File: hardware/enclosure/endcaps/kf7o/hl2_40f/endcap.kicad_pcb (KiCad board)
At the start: 2 copper layers, 106 x 40 mm, 22 parts, among them U1 IS31AP4996

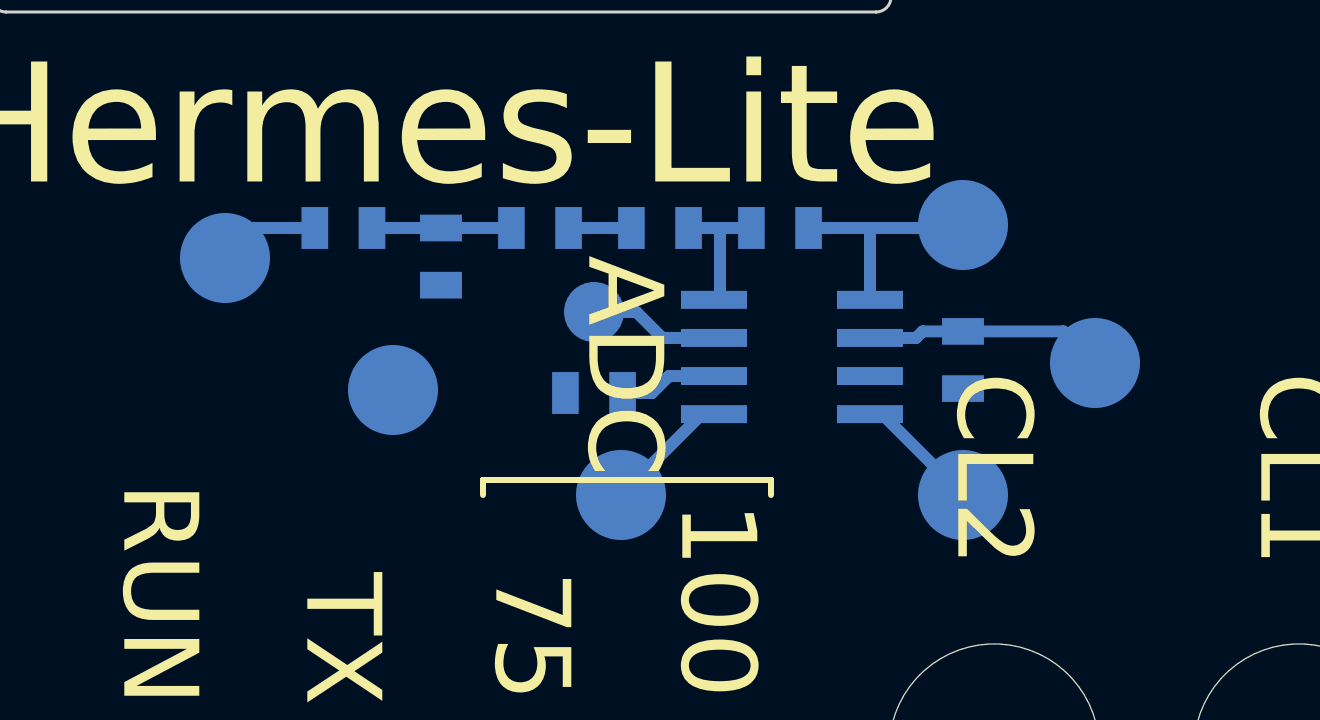
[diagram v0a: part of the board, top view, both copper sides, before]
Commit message: Add LPF for fan on latest end plates
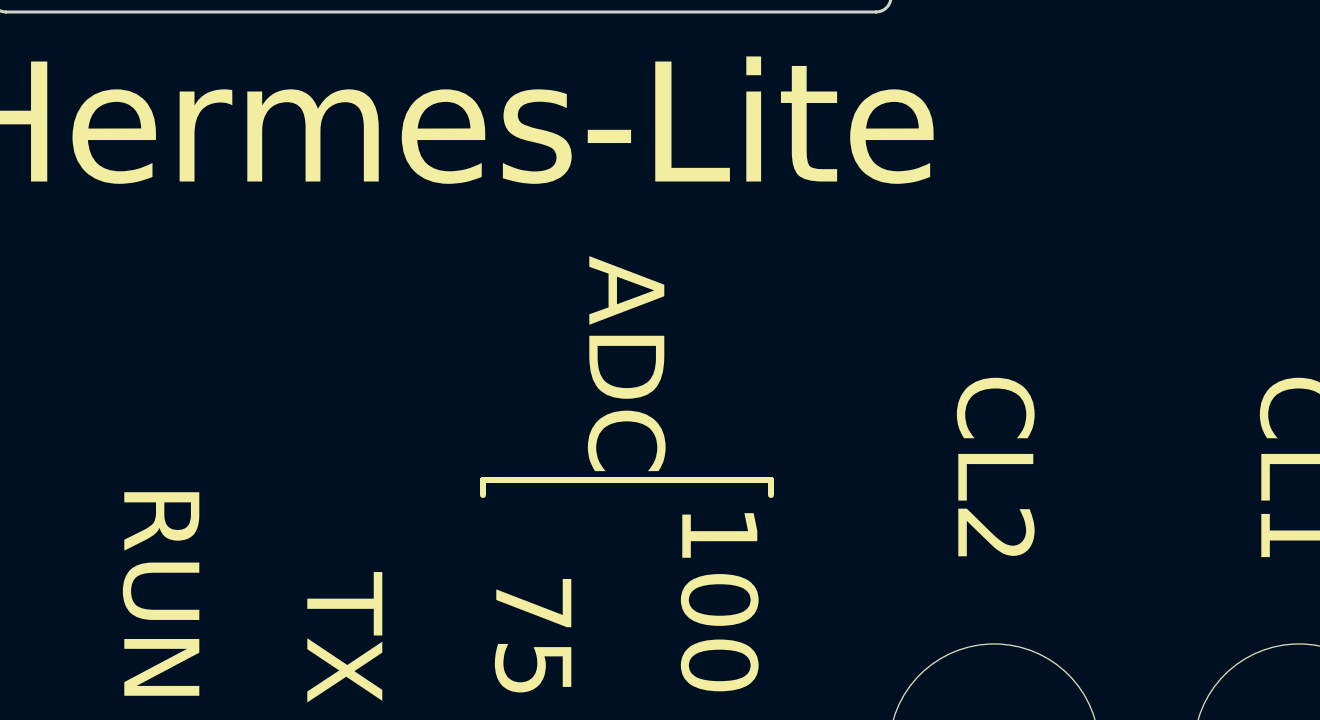
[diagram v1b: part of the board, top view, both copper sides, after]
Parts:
- removed C1, C4: 1uF, endcaplib:SMD-0805
- removed C2: 0.1uF, endcaplib:SMD-0805
- removed C3: 0.47uF, endcaplib:SMD-0805
- removed R1: 220, endcaplib:SMD-0805
- removed R2, R3: 20K, endcaplib:SMD-0805
- removed TP1: PWM, TestPoint:TestPoint_Pad_D3.0mm
- removed TP2: GND, TestPoint:TestPoint_Pad_D3.0mm
- removed TP3: 3.3V, TestPoint:TestPoint_Pad_D3.0mm
- removed TP4: A+, TestPoint:TestPoint_Pad_D3.0mm
- removed TP5: A-, TestPoint:TestPoint_Pad_D3.0mm
- removed TP6: SD, TestPoint:TestPoint_Pad_D3.0mm
- removed TP7: IN+, TestPoint:TestPoint_Pad_D2.0mm
- removed U1: IS31AP4996, endcaplib:SOIC-8
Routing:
- net Net-(C4-Pad2): track 8.03 -> 0.00 mm
- net Net-(R3-Pad1): track 7.58 -> 0.00 mm
- net Net-(C1-Pad1): track 4.65 -> 0.00 mm
- net Net-(R2-Pad1): track 4.57 -> 0.00 mm
- net Net-(TP7-Pad1): track 4.36 -> 0.00 mm
- net Net-(TP4-Pad1): track 4.22 -> 0.00 mm
- net Net-(TP6-Pad1): track 4.22 -> 0.00 mm
- net Net-(R1-Pad2): track 3.41 -> 0.00 mm
- net Net-(C3-Pad1): track 3.28 -> 0.00 mm
- net Net-(C2-Pad1): track 2.09 -> 0.00 mm
